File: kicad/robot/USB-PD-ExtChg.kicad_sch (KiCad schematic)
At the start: 28 parts, among them J1 USBC_Receptacle_SMD_RA, Q3 YJL3416A, Q4 YJL3416A, U18 AP33771DKZ-13

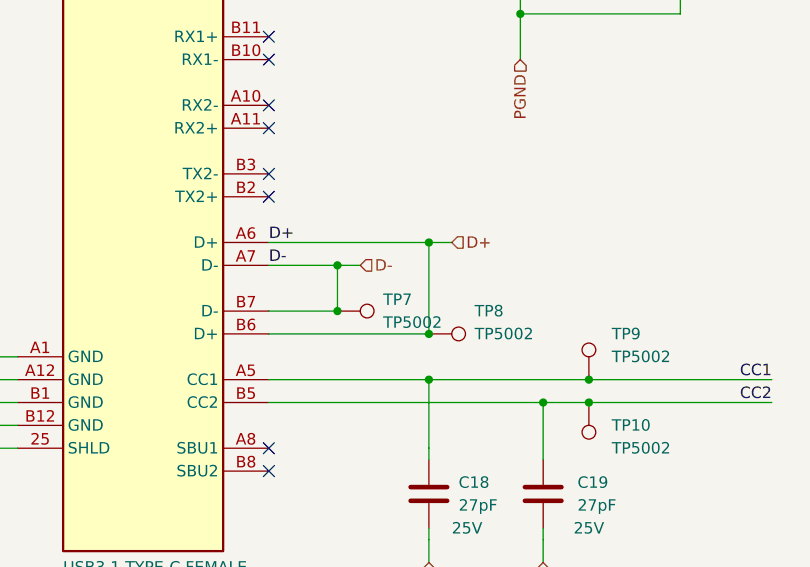
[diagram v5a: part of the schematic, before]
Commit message: Removed unused Dn/DP pins
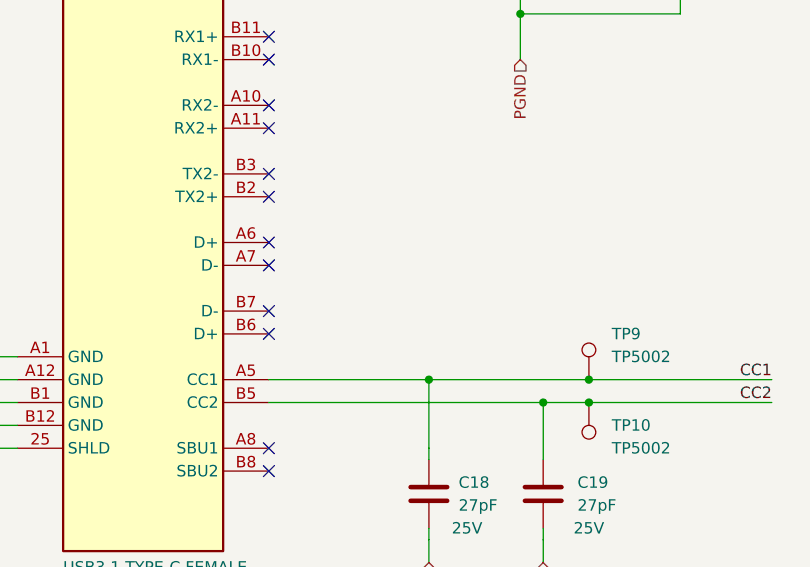
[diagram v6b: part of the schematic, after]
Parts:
- removed TP7, TP8: TP5002, TestPoint:KEYSTONE_5002, symbol Connector:TestPoint
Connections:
- net D+: no longer names the net of J1.A6 (D+)
- net D+: no longer J1.B6 (D+)
- net D-: no longer names the net of J1.A7 (D-)
- net D-: no longer J1.B7 (D-)
- no-connect marks 12 -> 16
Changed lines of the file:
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@@
 (kicad_sch (version 20211123) (generator eeschema)
   (paper "A2")
-  (junction (at 190.5 171.45) (diameter 0) (color 0 0 0 0)
-  )
   (junction (at 307.34 133.35) (diameter 0) (color 0 0 0 0)
   )
@@
   (junction (at 187.96 130.81) (diameter 0) (color 0 0 0 0)
   )
-  (junction (at 200.66 179.07) (diameter 0) (color 0 0 0 0)
-  )
   (junction (at 228.6 125.73) (diameter 0) (color 0 0 0 0)
   )
@@
   (junction (at 341.63 196.85) (diameter 0) (color 0 0 0 0)
   )
-  (junction (at 200.66 168.91) (diameter 0) (color 0 0 0 0)
-  )
   (junction (at 152.4 191.77) (diameter 0) (color 0 0 0 0)
   )
@@
   )
   (junction (at 307.34 125.73) (diameter 0) (color 0 0 0 0)
-  )
-  (junction (at 190.5 176.53) (diameter 0) (color 0 0 0 0)
   )
   (junction (at 152.4 184.15) (diameter 0) (color 0 0 0 0)
@@
   (no_connect (at 288.29 207.01))
   (no_connect (at 182.88 191.77))
+  (no_connect (at 182.88 168.91))
   (no_connect (at 309.245 191.77))
   (no_connect (at 182.88 194.31))
+  (no_connect (at 182.88 176.53))
   (no_connect (at 182.88 153.67))
   (no_connect (at 182.88 148.59))
   (no_connect (at 182.88 163.83))
   (no_connect (at 182.88 161.29))
+  (no_connect (at 182.88 179.07))
+  (no_connect (at 182.88 171.45))
   (no_connect (at 182.88 140.97))
   (no_connect (at 182.88 156.21))
@@
     (stroke (width 0) (type default) (color 0 0 0 0))
   )
-  (wire (pts (xy 200.66 168.91) (xy 182.88 168.91))
-    (stroke (width 0.254) (type default) (color 0 0 0 0))
-  )
   (wire (pts (xy 297.18 163.83) (xy 316.865 163.83))
     (stroke (width 0) (type default) (color 0 0 0 0))
@@
     (stroke (width 0) (type default) (color 0 0 0 0))
   )
-  (wire (pts (xy 190.5 176.53) (xy 190.5 171.45))
-    (stroke (width 0.254) (type default) (color 0 0 0 0))
-  )
   (wire (pts (xy 187.96 125.73) (xy 210.82 125.73))
     (stroke (width 0.254) (type default) (color 0 0 0 0))
@@
     (stroke (width 0) (type default) (color 0 0 0 0))
   )
-  (wire (pts (xy 200.66 168.91) (xy 203.2 168.91))
-    (stroke (width 0) (type default) (color 0 0 0 0))
-  )
   (wire (pts (xy 218.44 186.69) (xy 238.76 186.69))
     (stroke (width 0) (type default) (color 0 0 0 0))
@@
     (stroke (width 0) (type default) (color 0 0 0 0))
   )
-  (wire (pts (xy 182.88 179.07) (xy 200.66 179.07))
-    (stroke (width 0.254) (type default) (color 0 0 0 0))
-  )
   (wire (pts (xy 316.865 163.83) (xy 316.865 165.735))
     (stroke (width 0) (type default) (color 0 0 0 0))
@@
     (stroke (width 0.254) (type default) (color 0 0 0 0))
   )
-  (wire (pts (xy 190.5 171.45) (xy 193.04 171.45))
-    (stroke (width 0) (type default) (color 0 0 0 0))
-  )
   (wire (pts (xy 152.4 189.23) (xy 152.4 191.77))
     (stroke (width 0.254) (type default) (color 0 0 0 0))
@@
     (stroke (width 0) (type default) (color 0 0 0 0))
   )
-  (wire (pts (xy 200.66 179.07) (xy 200.66 168.91))
-    (stroke (width 0.254) (type default) (color 0 0 0 0))
-  )
   (wire (pts (xy 336.55 125.73) (xy 336.55 127.635))
     (stroke (width 0) (type default) (color 0 0 0 0))
@@
     (stroke (width 0.254) (type default) (color 0 0 0 0))
   )
-  (wire (pts (xy 182.88 176.53) (xy 190.5 176.53))
-    (stroke (width 0.254) (type default) (color 0 0 0 0))
-  )
   (wire (pts (xy 200.66 184.15) (xy 218.44 184.15))
     (stroke (width 0.254) (type default) (color 0 0 0 0))
@@
   (wire (pts (xy 337.185 184.15) (xy 337.185 189.23))
     (stroke (width 0) (type default) (color 0 0 0 0))
-  )
-  (wire (pts (xy 190.5 171.45) (xy 182.88 171.45))
-    (stroke (width 0.254) (type default) (color 0 0 0 0))
   )
   (wire (pts (xy 346.075 186.69) (xy 353.06 186.69))
@@
     (effects (font (size 1.27 1.27)) (justify left bottom))
   )
-  (label "D+" (at 182.88 168.91 0)
-    (effects (font (size 1.27 1.27)) (justify left bottom))
-  )
   (label "CC1" (at 238.76 184.15 180)
     (effects (font (size 1.27 1.27)) (justify right bottom))
@@
     (effects (font (size 1.27 1.27)) (justify right bottom))
   )
-  (label "D-" (at 182.88 171.45 0)
-    (effects (font (size 1.27 1.27)) (justify left bottom))
-  )
   (hierarchical_label "VOUT" (shape input) (at 347.98 125.73 0)
     (effects (font (size 1.27 1.27)) (justify left))
@@
     (effects (font (size 1.27 1.27)) (justify right))
   )
-  (hierarchical_label "D-" (shape input) (at 193.04 171.45 0)
-    (effects (font (size 1.27 1.27)) (justify left))
-  )
   (hierarchical_label "AGND" (shape input) (at 263.525 213.36 180)
     (effects (font (size 1.27 1.27)) (justify right))
@@
   (hierarchical_label "AGND" (shape input) (at 295.91 243.84 180)
     (effects (font (size 1.27 1.27)) (justify right))
-  )
-  (hierarchical_label "D+" (shape input) (at 203.2 168.91 0)
-    (effects (font (size 1.27 1.27)) (justify left))
   )
   (symbol (lib_id "Device:C") (at 228.6 133.35 0) (unit 1)
@@
     )
     (property "Datasheet" "~" (id 3) (at 276.86 125.73 0)
-      (effects (font (size 1.27 1.27)) hide)
-    )
-    (pin "1")
-  )
-  (symbol (lib_id "Connector:TestPoint") (at 190.5 176.53 270) (unit 1)
-    (in_bom yes) (on_board yes) (fields_autoplaced)
-    (property "Reference" "TP7" (id 0) (at 195.58 175.2599 90)
-      (effects (font (size 1.27 1.27)) (justify left))
-    )
-    (property "Value" "TP5002" (id 1) (at 195.58 177.7999 90)
-      (effects (font (size 1.27 1.27)) (justify left))
-    )
-    (property "Footprint" "TestPoint:KEYSTONE_5002" (id 2) (at 190.5 181.61 0)
-      (effects (font (size 1.27 1.27)) hide)
-    )
-    (property "Datasheet" "~" (id 3) (at 190.5 181.61 0)
-      (effects (font (size 1.27 1.27)) hide)
-    )
-    (property "Description" "ExtC_D-" (id 4) (at 190.5 176.53 0)
-      (effects (font (size 1.27 1.27)) hide)
-    )
-    (property "Manufacturer" "Keystone Electronics" (id 5) (at 190.5 176.53 0)
-      (effects (font (size 1.27 1.27)) hide)
-    )
-    (property "Part Number" "5002" (id 6) (at 190.5 176.53 0)
       (effects (font (size 1.27 1.27)) hide)
     )
@@
     (pin "2")
   )
-  (symbol (lib_id "Connector:TestPoint") (at 200.66 179.07 270) (unit 1)
-    (in_bom yes) (on_board yes)
-    (property "Reference" "TP8" (id 0) (at 205.74 176.53 90)
-      (effects (font (size 1.27 1.27)) (justify left))
-    )
-    (property "Value" "TP5002" (id 1) (at 205.74 179.07 90)
-      (effects (font (size 1.27 1.27)) (justify left))
-    )
-    (property "Footprint" "TestPoint:KEYSTONE_5002" (id 2) (at 200.66 184.15 0)
-      (effects (font (size 1.27 1.27)) hide)
-    )
-    (property "Datasheet" "~" (id 3) (at 200.66 184.15 0)
-      (effects (font (size 1.27 1.27)) hide)
-    )
-    (property "Description" "ExtC_D+" (id 4) (at 200.66 179.07 0)
-      (effects (font (size 1.27 1.27)) hide)
-    )
-    (property "Manufacturer" "Keystone Electronics" (id 5) (at 200.66 179.07 0)
-      (effects (font (size 1.27 1.27)) hide)
-    )
-    (property "Part Number" "5002" (id 6) (at 200.66 179.07 0)
-      (effects (font (size 1.27 1.27)) hide)
-    )
-    (pin "1")
-  )
   (symbol (lib_id "Device:C") (at 200.66 196.85 0) (unit 1)

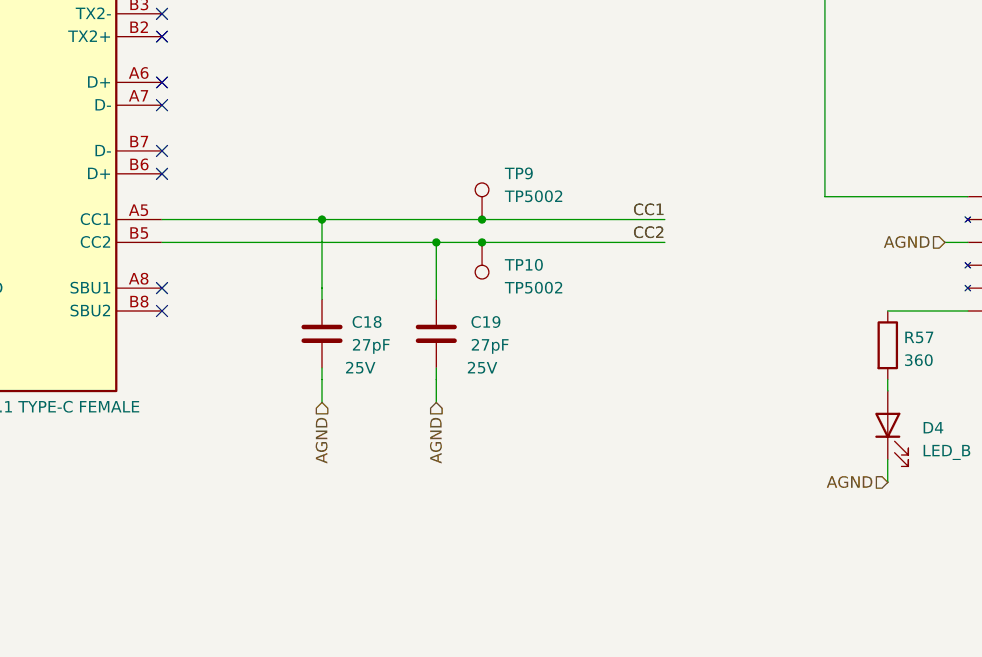
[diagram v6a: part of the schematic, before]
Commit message: Added ESD to CC lines
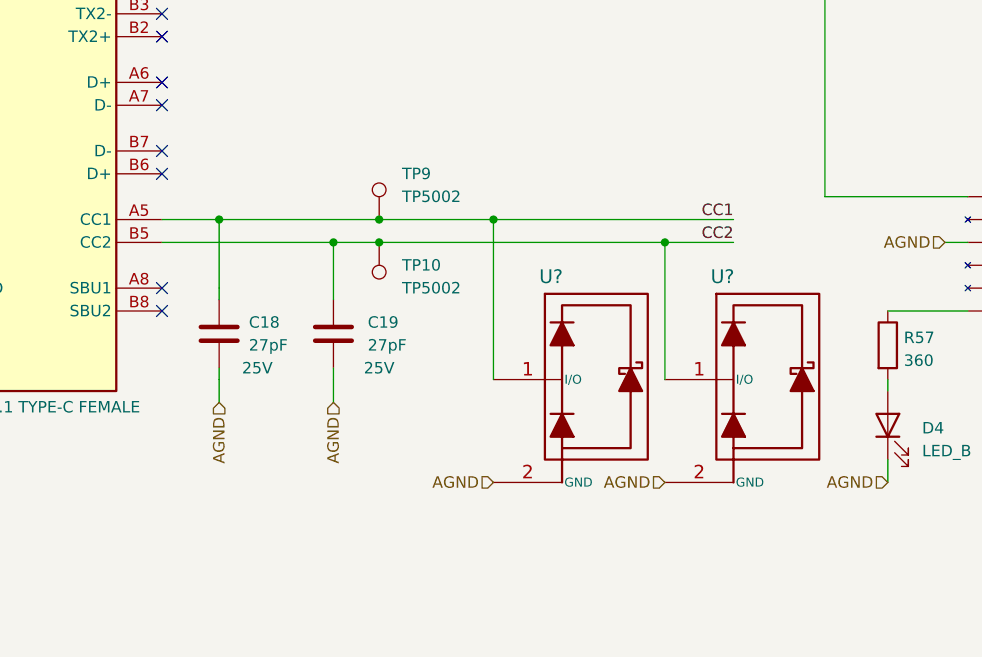
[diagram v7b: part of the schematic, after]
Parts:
- added U? (x2): TPD1E05U06, Package_X1SON:TPD1E05U06DPYR, symbol Diode:TPD1E05U06
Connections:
- net AGND: now also U?.2 (GND), U?.2 (GND)
- net CC1: now also U?.1 (I/O)
- net CC2: now also U?.1 (I/O)
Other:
- moved on the sheet: C18, C19, TP10, TP9
